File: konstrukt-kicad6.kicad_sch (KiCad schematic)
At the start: 0 parts

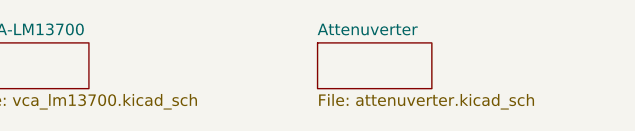
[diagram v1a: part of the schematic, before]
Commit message: Add circuitjs for verified blocks
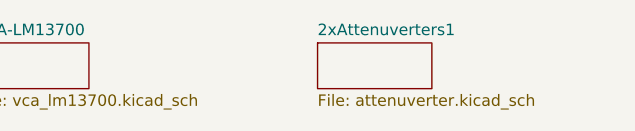
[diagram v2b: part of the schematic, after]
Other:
- sheet Attenuverter renamed 2xAttenuverters1
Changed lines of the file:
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@@
     (stroke (width 0.1524) (type solid) (color 0 0 0 0))
     (fill (color 0 0 0 0.0000))
-    (property "Sheet name" "Attenuverter" (id 0) (at 63.5 24.6884 0)
+    (property "Sheet name" "2xAttenuverters1" (id 0) (at 63.5 24.6884 0)
       (effects (font (size 1.27 1.27)) (justify left bottom))
     )
@@
       (reference "C?") (unit 1) (value "small??") (footprint "")
     )
+    (path "/a20b1572-4a1d-447e-be8c-a6218de04c26/34a597f2-4024-434d-a700-3301b9094bb7"
+      (reference "C?") (unit 1) (value "30p") (footprint "")
+    )
+    (path "/a20b1572-4a1d-447e-be8c-a6218de04c26/47f36d3b-551e-4ea4-812a-64631f60e3d8"
+      (reference "C?") (unit 1) (value "100n") (footprint "")
+    )
+    (path "/a20b1572-4a1d-447e-be8c-a6218de04c26/4c45c571-e206-437f-b692-ee4c0ba02415"
+      (reference "C?") (unit 1) (value "30p") (footprint "")
+    )
+    (path "/a20b1572-4a1d-447e-be8c-a6218de04c26/5bbf813c-9c17-4159-a225-af9681b70e83"
+      (reference "C?") (unit 1) (value "30p") (footprint "")
+    )
+    (path "/a20b1572-4a1d-447e-be8c-a6218de04c26/9496c012-4848-42fc-bdb6-48d4709e7bc2"
+      (reference "C?") (unit 1) (value "100n") (footprint "")
+    )
+    (path "/a20b1572-4a1d-447e-be8c-a6218de04c26/f13f0dc4-b9eb-4363-9108-67eefadcb2c9"
+      (reference "C?") (unit 1) (value "30p") (footprint "")
+    )
     (path "/a20b1572-4a1d-447e-be8c-a6218de04c26/252b7ce1-a59f-4e1b-b0a5-0ea97ff42d6c"
       (reference "D?") (unit 1) (value "LED_Green") (footprint "")
     )
+    (path "/a20b1572-4a1d-447e-be8c-a6218de04c26/4e6530eb-6e5e-46f5-ab6c-4d5e2db6060a"
+      (reference "D?") (unit 1) (value "D_TVS") (footprint "")
+    )
+    (path "/a20b1572-4a1d-447e-be8c-a6218de04c26/7a764438-b883-4fce-8d2c-39e969f073c9"
+      (reference "D?") (unit 1) (value "D_TVS") (footprint "")
+    )
+    (path "/a20b1572-4a1d-447e-be8c-a6218de04c26/c01f1119-c7bc-4e9f-9363-206a1c067449"
+      (reference "D?") (unit 1) (value "D_TVS") (footprint "")
+    )
+    (path "/a20b1572-4a1d-447e-be8c-a6218de04c26/c6e1d0a6-8dec-477c-a3b1-7b66b4e10d06"
+      (reference "D?") (unit 1) (value "D_TVS") (footprint "")
+    )
     (path "/a20b1572-4a1d-447e-be8c-a6218de04c26/da962cdb-b1cf-4a77-8dee-4c29b141f5dc"
       (reference "D?") (unit 1) (value "LED_Yellow") (footprint "")
     )
+    (path "/a20b1572-4a1d-447e-be8c-a6218de04c26/dadd5976-0abb-4b46-90a5-234b3daf3191"
+      (reference "D?") (unit 1) (value "LED_Green") (footprint "")
+    )
+    (path "/a20b1572-4a1d-447e-be8c-a6218de04c26/ff6e26f9-06cf-43c7-972e-294e5ccf8404"
+      (reference "D?") (unit 1) (value "LED_Yellow") (footprint "")
+    )
+    (path "/a20b1572-4a1d-447e-be8c-a6218de04c26/61bd750c-d666-47c5-a035-f0b3fb6f4f6e"
+      (reference "H?") (unit 1) (value "${SHEETNAME}_1_In") (footprint "")
+    )
+    (path "/a20b1572-4a1d-447e-be8c-a6218de04c26/8748612c-7cdf-4336-9478-d7409bea2883"
+      (reference "H?") (unit 1) (value "${SHEETNAME}_2_Out") (footprint "")
+    )
+    (path "/a20b1572-4a1d-447e-be8c-a6218de04c26/a38aafa9-7b28-424a-8443-87debfc3f21d"
+      (reference "H?") (unit 1) (value "${SHEETNAME}_2_In") (footprint "")
+    )
+    (path "/a20b1572-4a1d-447e-be8c-a6218de04c26/e33e5532-e0e5-476f-843a-917cc002438f"
+      (reference "H?") (unit 1) (value "${SHEETNAME}_1_Out") (footprint "")
+    )
     (path "/cd541d08-aa8e-4180-93a3-c37a39586684/6647148d-8c8c-4478-9c91-47698f705480"
       (reference "Q?") (unit 1) (value "Q_PNP_EBC") (footprint "")
     )
+    (path "/a20b1572-4a1d-447e-be8c-a6218de04c26/03202f99-4a10-4e49-a992-caa005f008cd"
+      (reference "R?") (unit 1) (value "100K") (footprint "")
+    )
     (path "/cd541d08-aa8e-4180-93a3-c37a39586684/053304b4-6d2e-44fa-912f-91a390d196c8"
       (reference "R?") (unit 1) (value "100K") (footprint "")
+    )
+    (path "/a20b1572-4a1d-447e-be8c-a6218de04c26/0fe6382c-8836-4226-8f00-ab4b260ee474"
+      (reference "R?") (unit 1) (value "1K") (footprint "")
     )
     (path "/a20b1572-4a1d-447e-be8c-a6218de04c26/1050dbb5-1e4e-4535-8d33-d9edb343b186"
@@
       (reference "R?") (unit 1) (value "30K") (footprint "")
     )
+    (path "/a20b1572-4a1d-447e-be8c-a6218de04c26/50662059-9443-4b89-b60e-61ce96a7155c"
+      (reference "R?") (unit 1) (value "100K") (footprint "")
+    )
     (path "/cd541d08-aa8e-4180-93a3-c37a39586684/50f4ac17-3af7-4274-af76-3aee1e2b9598"
       (reference "R?") (unit 1) (value "30K") (footprint "")
     )
+    (path "/a20b1572-4a1d-447e-be8c-a6218de04c26/551167a4-48e8-4ee7-b5d4-153b4a0902bc"
+      (reference "R?") (unit 1) (value "100K") (footprint "")
+    )
     (path "/a20b1572-4a1d-447e-be8c-a6218de04c26/5ba17802-7cc1-4128-8654-e64523892643"
       (reference "R?") (unit 1) (value "100K") (footprint "")
@@
       (reference "R?") (unit 1) (value "10K") (footprint "")
     )
+    (path "/a20b1572-4a1d-447e-be8c-a6218de04c26/7b890697-ffc4-49fb-92a8-bd6079d0e58f"
+      (reference "R?") (unit 1) (value "1K") (footprint "")
+    )
     (path "/cd541d08-aa8e-4180-93a3-c37a39586684/867b2222-b381-450c-9e6c-9c5fb617fc2b"
       (reference "R?") (unit 1) (value "5K") (footprint "")
@@
       (reference "R?") (unit 1) (value "100K") (footprint "")
     )
+    (path "/a20b1572-4a1d-447e-be8c-a6218de04c26/910e4c3b-4298-4ad3-909c-881e33bb9bdd"
+      (reference "R?") (unit 1) (value "20K") (footprint "")
+    )
+    (path "/a20b1572-4a1d-447e-be8c-a6218de04c26/93c0ec29-a9ea-4255-89ea-17e6f418de3c"
+      (reference "R?") (unit 1) (value "100K") (footprint "")
+    )
     (path "/cd541d08-aa8e-4180-93a3-c37a39586684/969e688e-089c-4b54-9749-ce78da9cfafa"
       (reference "R?") (unit 1) (value "680") (footprint "")
@@
       (reference "R?") (unit 1) (value "100K") (footprint "")
     )
+    (path "/a20b1572-4a1d-447e-be8c-a6218de04c26/a354070e-37fa-4786-86df-38ceb506344c"
+      (reference "R?") (unit 1) (value "100K") (footprint "")
+    )
     (path "/a20b1572-4a1d-447e-be8c-a6218de04c26/b3600d1b-b73b-4868-a7ce-cc8d221f18e7"
+      (reference "R?") (unit 1) (value "100K") (footprint "")
+    )
+    (path "/a20b1572-4a1d-447e-be8c-a6218de04c26/b827ccba-80c1-435b-ae69-79463aa016e3"
       (reference "R?") (unit 1) (value "100K") (footprint "")
     )
@@
       (reference "R?") (unit 1) (value "1K") (footprint "")
     )
+    (path "/a20b1572-4a1d-447e-be8c-a6218de04c26/c570ec2f-b496-4c9a-9f04-1971e51d8537"
+      (reference "R?") (unit 1) (value "470") (footprint "")
+    )
     (path "/a20b1572-4a1d-447e-be8c-a6218de04c26/ddc0f814-9f71-4673-9bc4-b352a0778f13"
       (reference "R?") (unit 1) (value "100K") (footprint "")
@@
     )
     (path "/a20b1572-4a1d-447e-be8c-a6218de04c26/ff107d2c-0d2e-4831-ade1-ae7b97e64c68"
-      (reference "R?") (unit 1) (value "330") (footprint "")
+      (reference "R?") (unit 1) (value "470") (footprint "")
     )
     (path "/cd541d08-aa8e-4180-93a3-c37a39586684/002006de-84f4-4c9a-8275-c47c18f21d2a"
@@
       (reference "RV?") (unit 1) (value "B100K") (footprint "")
     )
+    (path "/a20b1572-4a1d-447e-be8c-a6218de04c26/5fba8a87-c932-4b64-97a5-a93715f5c5cf"
+      (reference "RV?") (unit 1) (value "B100K") (footprint "")
+    )
     (path "/cd541d08-aa8e-4180-93a3-c37a39586684/74b71ea9-3493-4b5d-92ad-a382abc269aa"
       (reference "RV?") (unit 1) (value "100K multiturn") (footprint "")
     )
+    (path "/a20b1572-4a1d-447e-be8c-a6218de04c26/e93c5acb-f4d4-40fa-9689-d6636a140faf"
+      (reference "RV?") (unit 1) (value "B100K") (footprint "")
+    )
     (path "/cd541d08-aa8e-4180-93a3-c37a39586684/0ad5b807-adf8-49d7-b6c2-c38c814433d2"
       (reference "U?") (unit 1) (value "MCP6004") (footprint "")
     )
-    (path "/a20b1572-4a1d-447e-be8c-a6218de04c26/3cd517ff-9acd-4d38-9cb1-749ae80e9f18"
-      (reference "U?") (unit 1) (value "MCP6002-xSN") (footprint "")
-    )
     (path "/cd541d08-aa8e-4180-93a3-c37a39586684/8ee80077-4be8-4985-96f5-73fe0feb5ac1"
       (reference "U?") (unit 1) (value "LM13700") (footprint "")
@@
       (reference "U?") (unit 1) (value "MCP6004") (footprint "")
     )
+    (path "/a20b1572-4a1d-447e-be8c-a6218de04c26/f8302bd9-1786-4d45-b3d2-daa4da3578bd"
+      (reference "U?") (unit 1) (value "MCP6004") (footprint "")
+    )
     (path "/cd541d08-aa8e-4180-93a3-c37a39586684/3b8b2d08-b1d6-41f8-8d3a-ed412635442f"
       (reference "U?") (unit 2) (value "LM13700") (footprint "")
@@
       (reference "U?") (unit 2) (value "TL072") (footprint "")
     )
-    (path "/a20b1572-4a1d-447e-be8c-a6218de04c26/ec2d45cd-68bd-4fe2-957b-099479be35c9"
-      (reference "U?") (unit 2) (value "MCP6002-xSN") (footprint "")
+    (path "/a20b1572-4a1d-447e-be8c-a6218de04c26/d7fe3d8f-d48a-4193-a9f7-885e8d2d6a10"
+      (reference "U?") (unit 2) (value "MCP6004") (footprint "")
     )
     (path "/a20b1572-4a1d-447e-be8c-a6218de04c26/52394d72-5468-46f9-acce-f4fa96c3b49f"
@@
       (reference "U?") (unit 3) (value "LM13700") (footprint "")
     )
-    (path "/a20b1572-4a1d-447e-be8c-a6218de04c26/bf0011e1-51ed-41af-916b-5b9f2edc2cbf"
-      (reference "U?") (unit 3) (value "MCP6002-xSN") (footprint "")
+    (path "/a20b1572-4a1d-447e-be8c-a6218de04c26/aa0ccd33-e64f-4b82-bb45-d0310bc7a320"
+      (reference "U?") (unit 3) (value "MCP6004") (footprint "")
+    )
+    (path "/a20b1572-4a1d-447e-be8c-a6218de04c26/7e6b588d-5ac8-4a6b-878a-2ea1960e690f"
+      (reference "U?") (unit 4) (value "MCP6004") (footprint "")
     )
     (path "/cd541d08-aa8e-4180-93a3-c37a39586684/bd54bb00-f89b-4f8b-a7e3-c5eb11570bcc"
@@
       (reference "U?") (unit 5) (value "LM13700") (footprint "")
     )
-  )
+    (path "/a20b1572-4a1d-447e-be8c-a6218de04c26/8a75e787-166d-4c94-bcc8-35496d507e3a"
+      (reference "U?") (unit 5) (value "MCP6004") (footprint "")
+    )
+  )

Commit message: Attenuverter board wip
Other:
- sheet 2xAttenuverters1 ports: added +4.5V, +9V, GND; removed none

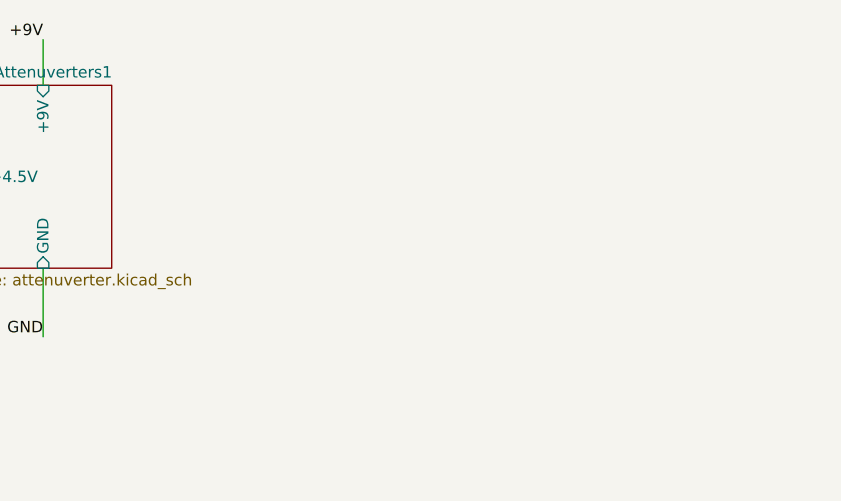
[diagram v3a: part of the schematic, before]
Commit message: Attenuverters laid out
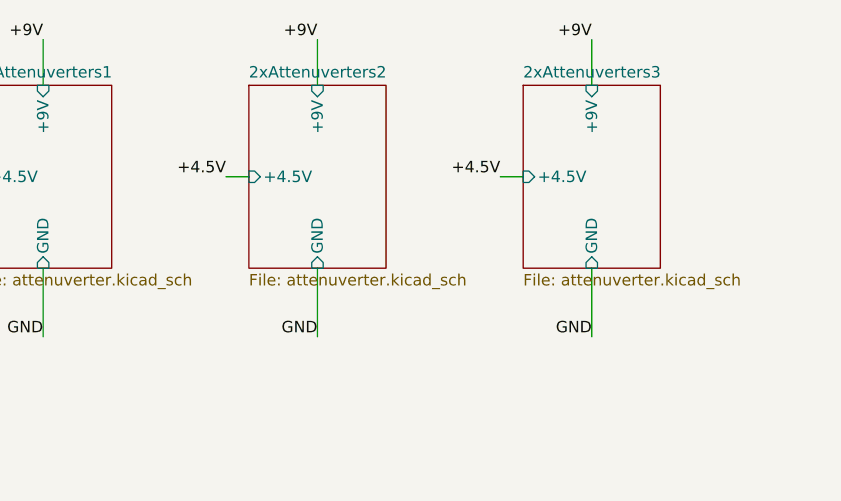
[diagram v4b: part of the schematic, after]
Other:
- added sheet 2xAttenuverters2 (attenuverter.kicad_sch)
- added sheet 2xAttenuverters3 (attenuverter.kicad_sch)

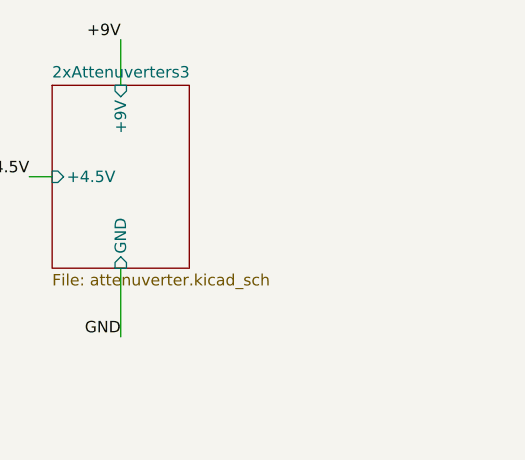
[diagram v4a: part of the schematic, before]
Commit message: VCF schem capture
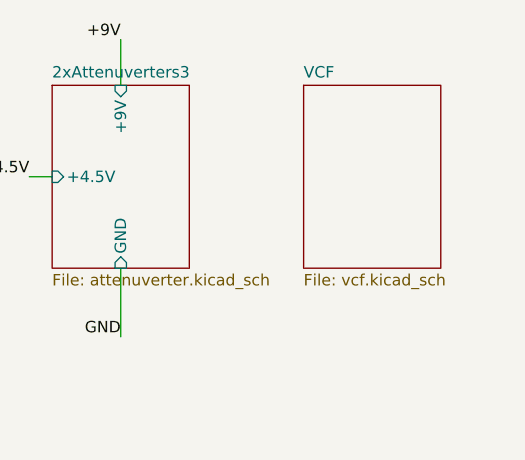
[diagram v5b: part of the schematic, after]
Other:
- added sheet VCF (vcf.kicad_sch)

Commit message: Start VCF layout
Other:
- sheet VCF ports: added +4.5V, +9V, GND; removed none
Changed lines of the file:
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@@
 (kicad_sch (version 20211123) (generator eeschema)
   (paper "A4")
+  (wire (pts (xy 149.86 35.56) (xy 152.4 35.56))
+    (stroke (width 0) (type default) (color 0 0 0 0))
+  )
   (wire (pts (xy 71.12 45.72) (xy 71.12 53.34))
     (stroke (width 0) (type default) (color 0 0 0 0))
@@
     (stroke (width 0) (type default) (color 0 0 0 0))
   )
+  (wire (pts (xy 160.02 20.32) (xy 160.02 25.4))
+    (stroke (width 0) (type default) (color 0 0 0 0))
+  )
+  (wire (pts (xy 160.02 45.72) (xy 160.02 53.34))
+    (stroke (width 0) (type default) (color 0 0 0 0))
+  )
   (wire (pts (xy 60.96 35.56) (xy 63.5 35.56))
     (stroke (width 0) (type default) (color 0 0 0 0))
@@
     (effects (font (size 1.27 1.27)) (justify right bottom))
   )
+  (label "+4.5V" (at 149.86 35.56 180)
+    (effects (font (size 1.27 1.27)) (justify right bottom))
+  )
+  (label "+9V" (at 160.02 20.32 180)
+    (effects (font (size 1.27 1.27)) (justify right bottom))
+  )
   (label "+4.5V" (at 121.92 35.56 180)
+    (effects (font (size 1.27 1.27)) (justify right bottom))
+  )
+  (label "GND" (at 160.02 53.34 180)
     (effects (font (size 1.27 1.27)) (justify right bottom))
   )
@@
     (property "Sheet file" "vcf.kicad_sch" (id 1) (at 152.4 46.3046 0)
       (effects (font (size 1.27 1.27)) (justify left top))
+    )
+    (pin "+4.5V" input (at 152.4 35.56 180)
+      (effects (font (size 1.27 1.27)) (justify left))
+    )
+    (pin "+9V" input (at 160.02 25.4 90)
+      (effects (font (size 1.27 1.27)) (justify right))
+    )
+    (pin "GND" input (at 160.02 45.72 270)
+      (effects (font (size 1.27 1.27)) (justify left))
     )
   )
@@
       (reference "C608") (unit 1) (value "220p") (footprint "Capacitor_SMD:C_0603_1608Metric_Pad1.08x0.95mm_HandSolder")
     )
-    (path "/83a74dc0-6079-45b8-a4be-0797c3d28006/08b70893-8354-4294-935b-5515bef7481a"
-      (reference "C609") (unit 1) (value "100n") (footprint "Capacitor_SMD:C_0603_1608Metric_Pad1.08x0.95mm_HandSolder")
-    )
     (path "/83a74dc0-6079-45b8-a4be-0797c3d28006/d836f5aa-cde8-4b76-914a-7f8a535510ce"
       (reference "C610") (unit 1) (value "1.2n") (footprint "Capacitor_SMD:C_0603_1608Metric_Pad1.08x0.95mm_HandSolder")
     )
-    (path "/83a74dc0-6079-45b8-a4be-0797c3d28006/738f3f7f-1a1c-4003-9605-9334deefae5c"
-      (reference "C611") (unit 1) (value "100n") (footprint "Capacitor_SMD:C_0603_1608Metric_Pad1.08x0.95mm_HandSolder")
-    )
     (path "/83a74dc0-6079-45b8-a4be-0797c3d28006/db2f67ec-8c33-4ac6-b862-c936d692f8de"
       (reference "C612") (unit 1) (value "100n") (footprint "Capacitor_SMD:C_0603_1608Metric_Pad1.08x0.95mm_HandSolder")
@@
       (reference "D605") (unit 1) (value "D_Zener") (footprint "Diode_SMD:D_SOD-123")
     )
+    (path "/83a74dc0-6079-45b8-a4be-0797c3d28006/67e3e1c2-9e09-4f0b-ace6-a54b97079b3f"
+      (reference "D606") (unit 1) (value "D_TVS") (footprint "Diode_SMD:D_SOD-323_HandSoldering")
+    )
     (path "/83a74dc0-6079-45b8-a4be-0797c3d28006/55105d8f-0df9-4d9a-b1b9-2099075188d8/32d54008-b532-40e2-bc99-b1e5f2074dc3"
       (reference "D701") (unit 1) (value "D_TVS") (footprint "Diode_SMD:D_SOD-323_HandSoldering")
@@
       (reference "H601") (unit 1) (value "Main_Out") (footprint "MountingHole:MountingHole_4.3mm_M4_Pad_TopBottom")
     )
+    (path "/83a74dc0-6079-45b8-a4be-0797c3d28006/e0c0e10c-57a8-44e4-8e84-0a3d4e739075"
+      (reference "H602") (unit 1) (value "In") (footprint "MountingHole:MountingHole_4.3mm_M4_Pad_TopBottom")
+    )
     (path "/83a74dc0-6079-45b8-a4be-0797c3d28006/55105d8f-0df9-4d9a-b1b9-2099075188d8/02107b5a-b040-42d0-ab0c-f87fd7dcbfe9"
       (reference "H701") (unit 1) (value "Freq_In") (footprint "MountingHole:MountingHole_4.3mm_M4_Pad_TopBottom")
@@
       (reference "U702") (unit 3) (value "TL072") (footprint "Package_SO:SOIC-8_3.9x4.9mm_P1.27mm")
     )
+    (path "/83a74dc0-6079-45b8-a4be-0797c3d28006/e859ea48-2399-46ea-81c3-33bbb9c73f68/1ce9ff63-f01d-43d9-aecb-ad83a8849d55"
+      (reference "U801") (unit 1) (value "TL074") (footprint "Package_SO:SOIC-14_3.9x8.7mm_P1.27mm")
+    )
+    (path "/83a74dc0-6079-45b8-a4be-0797c3d28006/e859ea48-2399-46ea-81c3-33bbb9c73f68/51189a05-878b-4bba-b62a-b73f72c9bcc4"
+      (reference "U801") (unit 2) (value "TL074") (footprint "Package_SO:SOIC-14_3.9x8.7mm_P1.27mm")
+    )
+    (path "/83a74dc0-6079-45b8-a4be-0797c3d28006/e859ea48-2399-46ea-81c3-33bbb9c73f68/b83dbe59-e690-4f32-a220-ddcd7bd4e782"
+      (reference "U801") (unit 3) (value "TL074") (footprint "Package_SO:SOIC-14_3.9x8.7mm_P1.27mm")
+    )
     (path "/83a74dc0-6079-45b8-a4be-0797c3d28006/e859ea48-2399-46ea-81c3-33bbb9c73f68/0e5e1ba0-6084-4790-bf39-8d10b7e5cf22"
-      (reference "U801") (unit 1) (value "TL074") (footprint "Package_SO:SOIC-14_3.9x8.7mm_P1.27mm")
-    )
-    (path "/83a74dc0-6079-45b8-a4be-0797c3d28006/e859ea48-2399-46ea-81c3-33bbb9c73f68/b83dbe59-e690-4f32-a220-ddcd7bd4e782"
-      (reference "U801") (unit 2) (value "TL074") (footprint "Package_SO:SOIC-14_3.9x8.7mm_P1.27mm")
-    )
-    (path "/83a74dc0-6079-45b8-a4be-0797c3d28006/e859ea48-2399-46ea-81c3-33bbb9c73f68/1ce9ff63-f01d-43d9-aecb-ad83a8849d55"
-      (reference "U801") (unit 3) (value "TL074") (footprint "Package_SO:SOIC-14_3.9x8.7mm_P1.27mm")
-    )
-    (path "/83a74dc0-6079-45b8-a4be-0797c3d28006/e859ea48-2399-46ea-81c3-33bbb9c73f68/51189a05-878b-4bba-b62a-b73f72c9bcc4"
       (reference "U801") (unit 4) (value "TL074") (footprint "Package_SO:SOIC-14_3.9x8.7mm_P1.27mm")
     )
@@
       (reference "U801") (unit 5) (value "TL074") (footprint "Package_SO:SOIC-14_3.9x8.7mm_P1.27mm")
     )
+    (path "/83a74dc0-6079-45b8-a4be-0797c3d28006/e859ea48-2399-46ea-81c3-33bbb9c73f68/27c28749-6d46-4887-b828-2777db93400f"
+      (reference "U802") (unit 1) (value "TL074") (footprint "Package_SO:SOIC-14_3.9x8.7mm_P1.27mm")
+    )
+    (path "/83a74dc0-6079-45b8-a4be-0797c3d28006/e859ea48-2399-46ea-81c3-33bbb9c73f68/1ad67449-49b4-43c1-a66a-e301477827d9"
+      (reference "U802") (unit 2) (value "TL074") (footprint "Package_SO:SOIC-14_3.9x8.7mm_P1.27mm")
+    )
+    (path "/83a74dc0-6079-45b8-a4be-0797c3d28006/e859ea48-2399-46ea-81c3-33bbb9c73f68/afce1519-1728-475a-95f4-15027fefb7e8"
+      (reference "U802") (unit 3) (value "TL074") (footprint "Package_SO:SOIC-14_3.9x8.7mm_P1.27mm")
+    )
     (path "/83a74dc0-6079-45b8-a4be-0797c3d28006/e859ea48-2399-46ea-81c3-33bbb9c73f68/6bf28202-654f-44d6-9af0-180717a23d19"
-      (reference "U802") (unit 1) (value "TL074") (footprint "Package_SO:SOIC-14_3.9x8.7mm_P1.27mm")
-    )
-    (path "/83a74dc0-6079-45b8-a4be-0797c3d28006/e859ea48-2399-46ea-81c3-33bbb9c73f68/afce1519-1728-475a-95f4-15027fefb7e8"
-      (reference "U802") (unit 2) (value "TL074") (footprint "Package_SO:SOIC-14_3.9x8.7mm_P1.27mm")
-    )
-    (path "/83a74dc0-6079-45b8-a4be-0797c3d28006/e859ea48-2399-46ea-81c3-33bbb9c73f68/27c28749-6d46-4887-b828-2777db93400f"
-      (reference "U802") (unit 3) (value "TL074") (footprint "Package_SO:SOIC-14_3.9x8.7mm_P1.27mm")
-    )
-    (path "/83a74dc0-6079-45b8-a4be-0797c3d28006/e859ea48-2399-46ea-81c3-33bbb9c73f68/1ad67449-49b4-43c1-a66a-e301477827d9"
       (reference "U802") (unit 4) (value "TL074") (footprint "Package_SO:SOIC-14_3.9x8.7mm_P1.27mm")
     )
